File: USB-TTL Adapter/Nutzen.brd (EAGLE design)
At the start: 100 x 100 mm, 4 parts, among them X1 22-23-2041, X3 22-23-2041

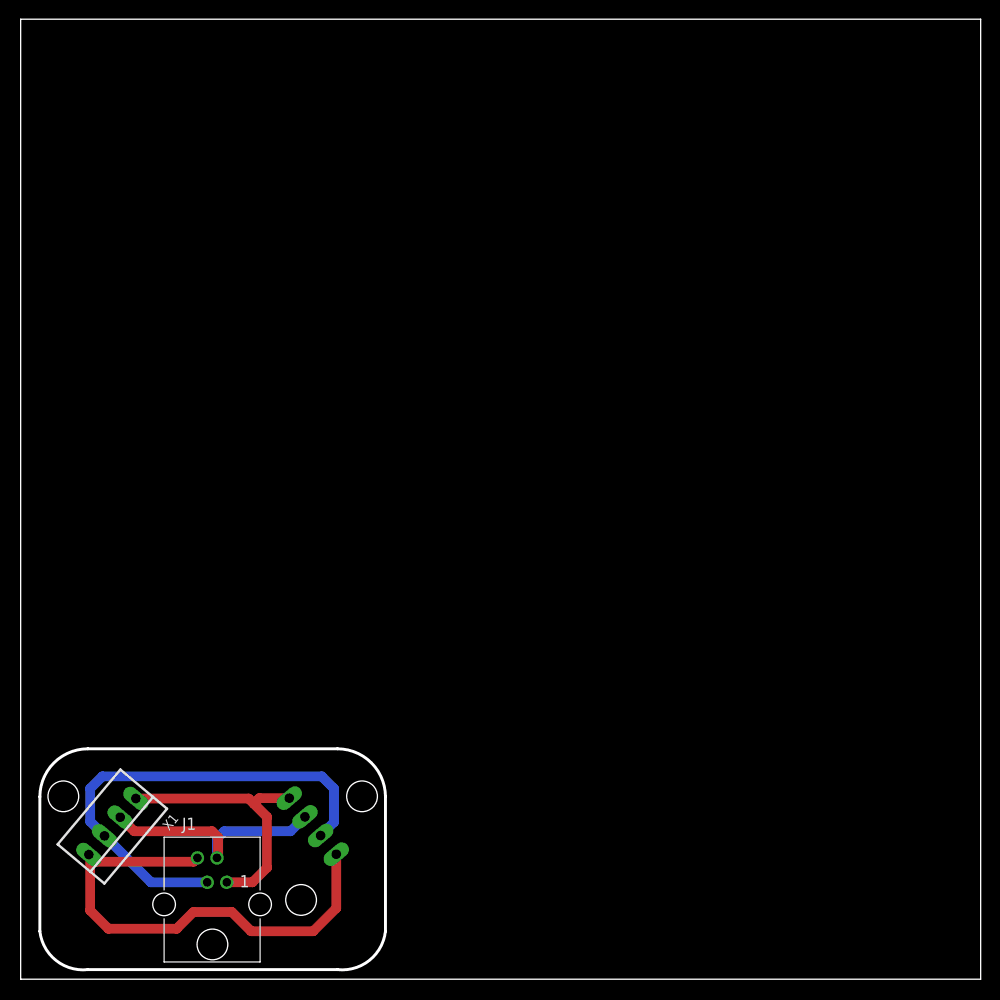
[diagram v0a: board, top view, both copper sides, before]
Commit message: 
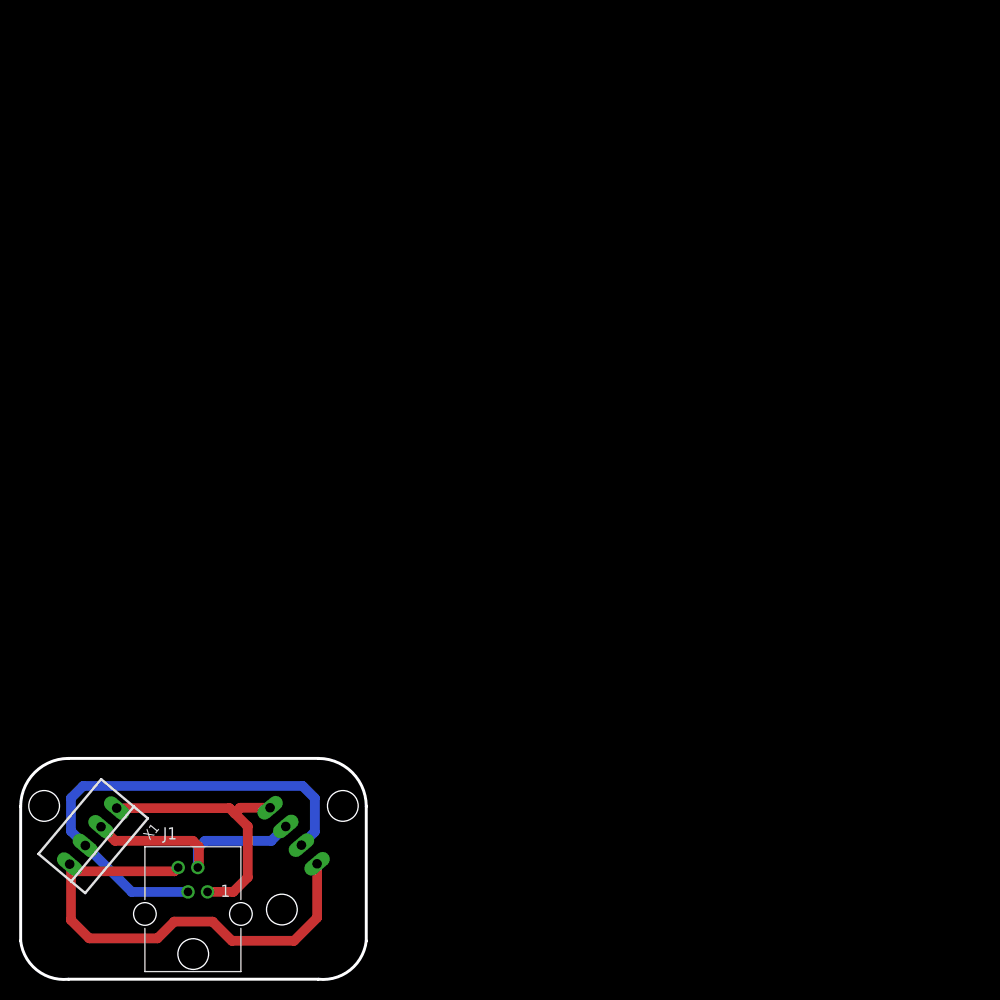
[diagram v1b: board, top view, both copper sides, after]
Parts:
- moved E$1 2.24 mm to (6.14, 4.25)
- moved J1 2.24 mm to (17.9, 6.79)
- moved X3 2.24 mm to (28.4, 14.9)
- moved X1 2.24 mm to (7.55, 14.9)
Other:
- board size 100 x 100 mm -> 36 x 23 mm
